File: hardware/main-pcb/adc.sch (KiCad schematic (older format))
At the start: 36 parts, among them U10 LP5907MFX-3.0, U11 LTC2292

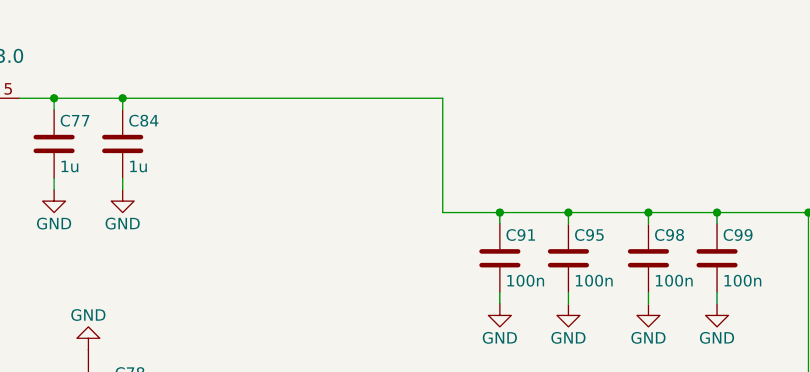
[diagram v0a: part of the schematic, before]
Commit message: pcb: connect ADC reference to voltage supply rail
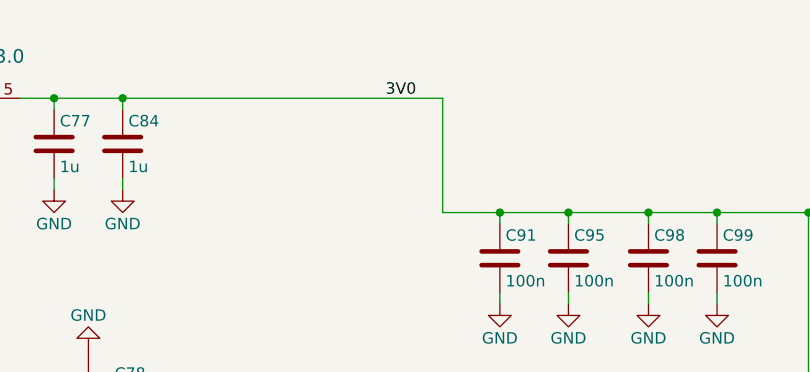
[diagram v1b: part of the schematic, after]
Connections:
- net 3V0: now also C77.1, C84.1, C91.1, C95.1, C98.1, C99.1, U10.5 (OUT), U11.10 (VDD), U11.18 (VDD), U11.63 (VDD), U11.7 (VDD)
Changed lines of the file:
@@
 EESchema Schematic File Version 4
 LIBS:fmcw-cache
-EELAYER 26 0
+EELAYER 30 0
 EELAYER END
 $Descr A4 11693 8268
@@
 Wire Wire Line
 	5650 1550 5950 1550
+Text Label 5150 1050 0    50   ~ 0
+3V0
 $EndSCHEMATC
